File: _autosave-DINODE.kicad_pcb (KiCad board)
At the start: 2 copper layers, 76.2 x 90.2 mm, 36 parts, among them J1 Barrel_Jack, J10 Conn_01x03_Male, J11 Conn_02x04_Odd_Even, J12 Conn_01x03_Female, J13 Conn_02x04_Odd_Even, J2 Conn_01x02_Male, J3 Conn_01x07, J4 Conn_01x16, J5 Conn_02x04_Odd_Even, J6 Conn_02x04_Odd_Even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

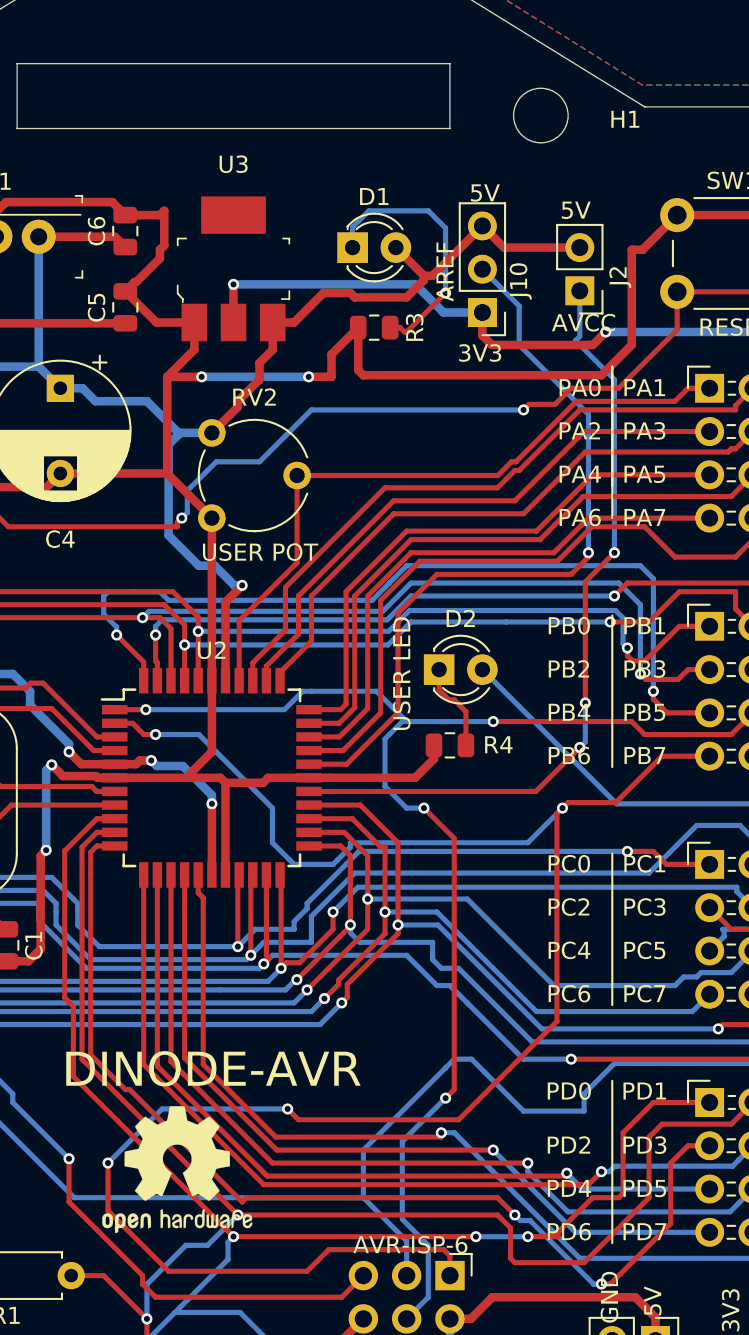
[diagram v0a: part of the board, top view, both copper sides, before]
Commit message: Addition of open-source logo
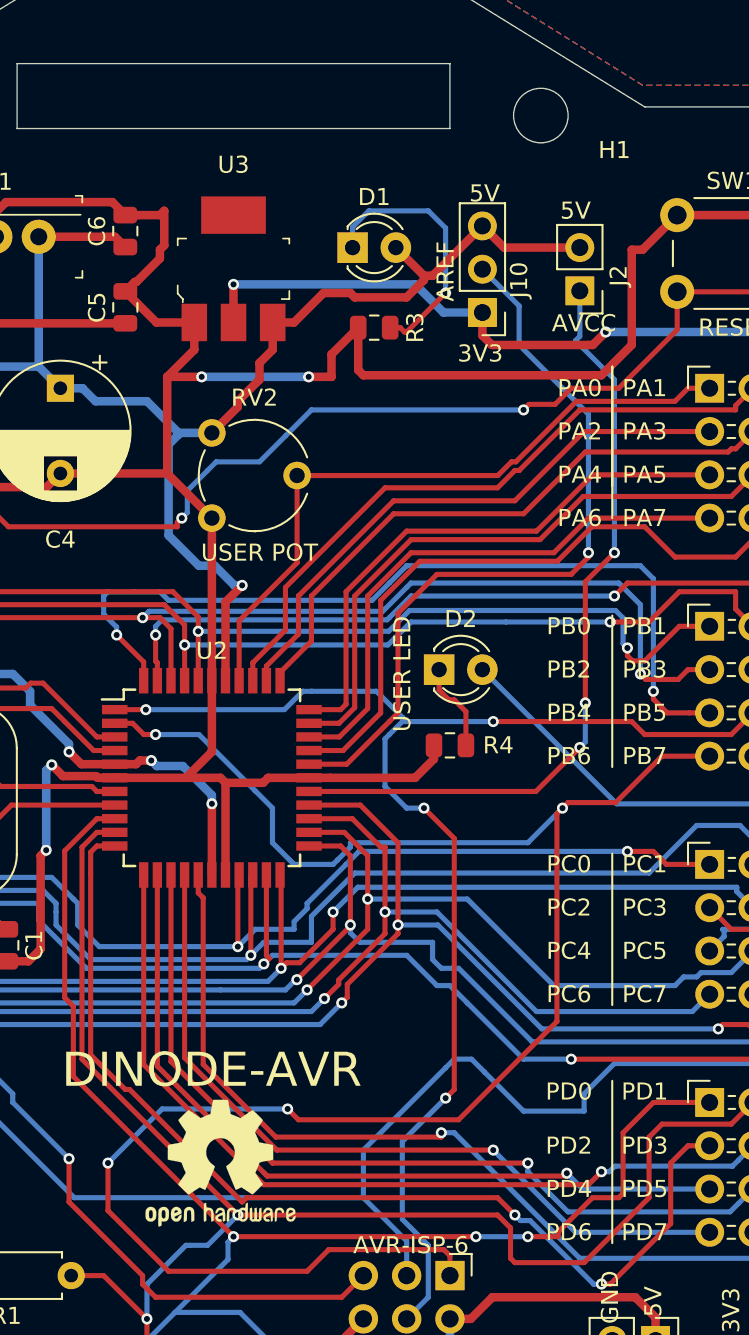
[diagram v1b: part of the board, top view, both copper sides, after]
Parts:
- moved REF** 2.57 mm to (123.7, 107.7)
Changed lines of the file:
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@@
   )
   (module Symbol:OSHW-Logo2_9.8x8mm_SilkScreen (layer F.Cu)
-    (at 121.158 108.077)
+    (at 123.698 107.696)
     (descr "Open Source Hardware Symbol")
     (tags "Logo Symbol OSHW")
@@
     (tags "mounting hole 3.2mm no annular m3")
     (attr virtual)
-    (fp_text reference H1 (at 4.953 0.254) (layer F.SilkS)
-      (effects (font (size 1 1) (thickness 0.15)))
-    )
+    (fp_text reference H1 (at 4.318 2.032) (layer F.SilkS)
+      (effects (font (size 1 1) (thickness 0.15)))
+    )
